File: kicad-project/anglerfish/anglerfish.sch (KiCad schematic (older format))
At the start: 3 parts

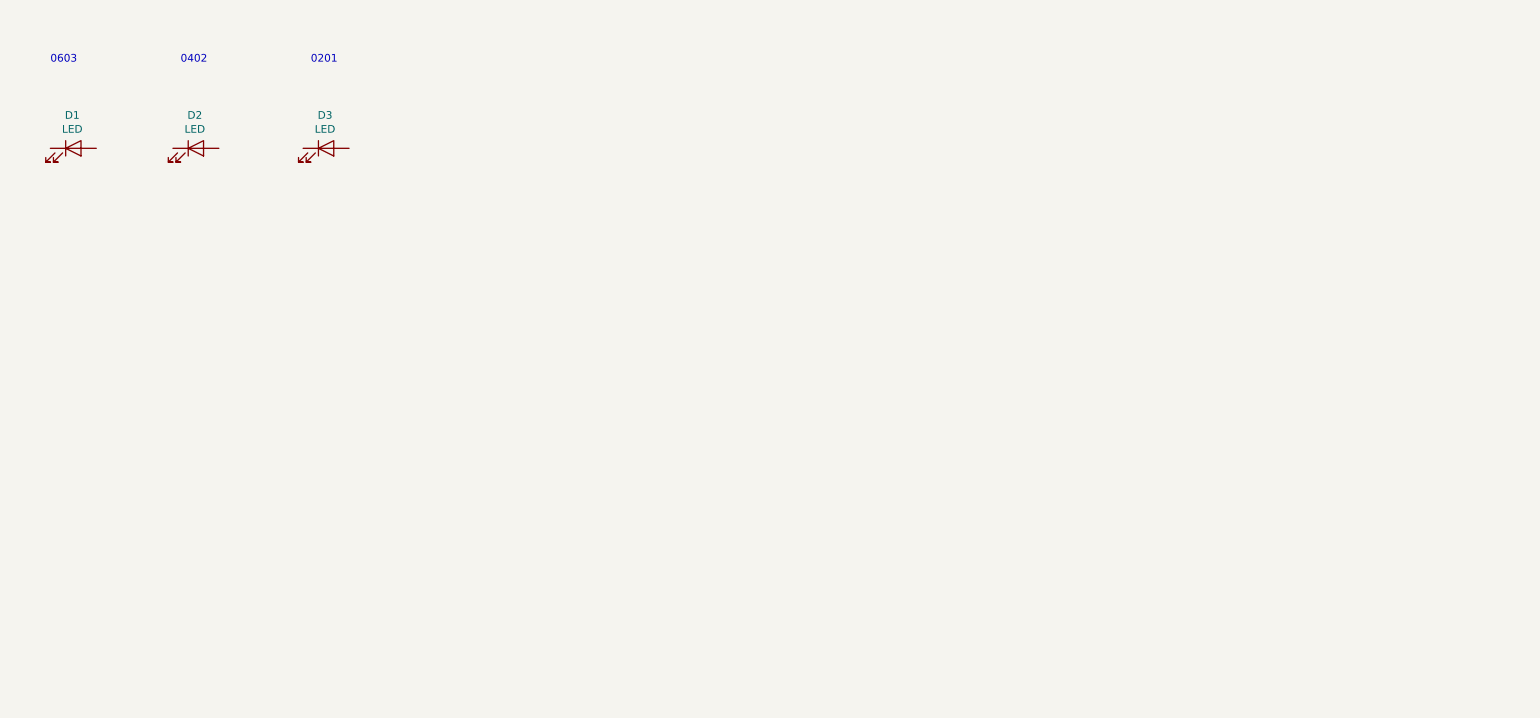
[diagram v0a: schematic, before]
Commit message: Added the 0402 whites. Also added the APA.
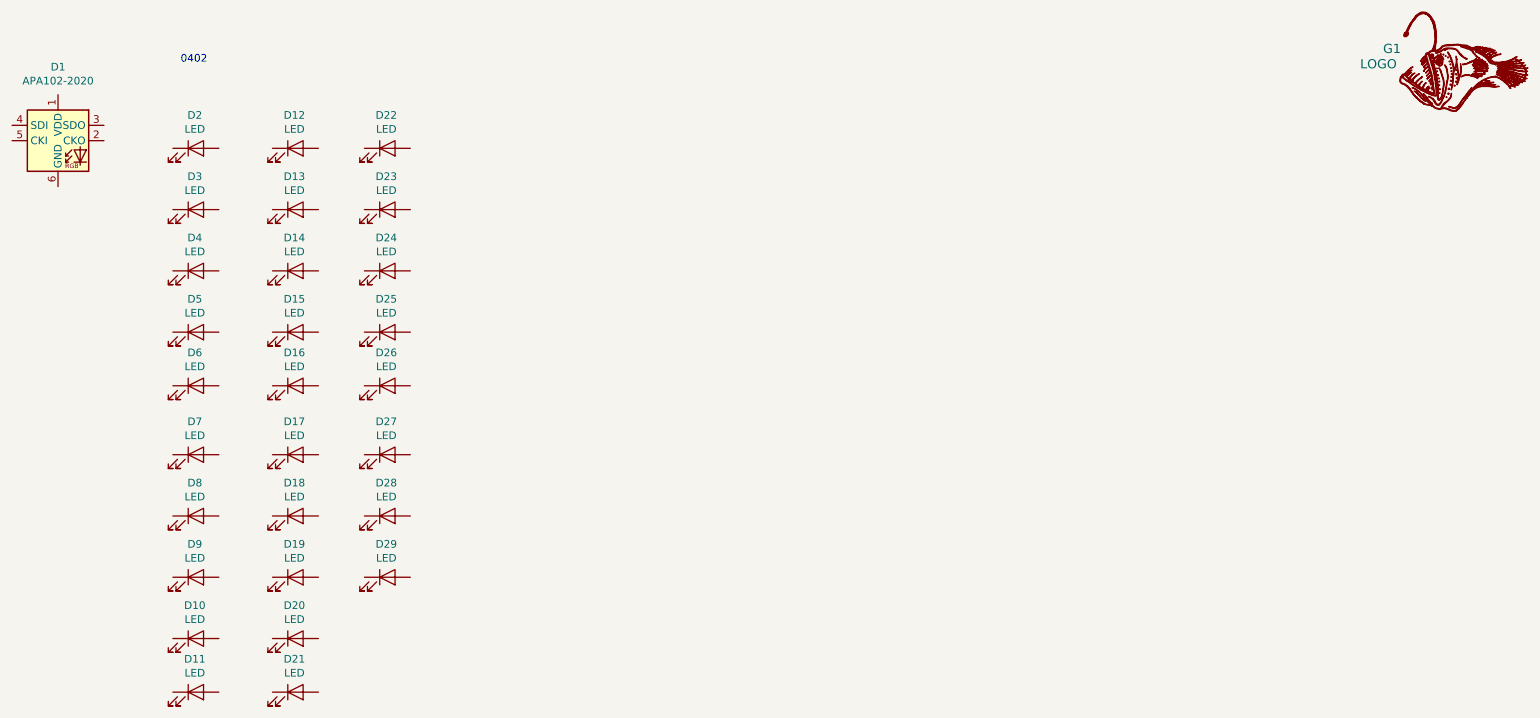
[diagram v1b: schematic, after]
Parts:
- removed D1: LED, LED_SMD:LED_0603_1608Metric, symbol Device:LED
- added D1: APA102-2020, LED_SMD:LED-APA102-2020, symbol LED:APA102-2020
- added D10, D11, D12, D13, D14, D15, D16, D17, D18, D19, D20, D21, D22, D23, D24, D25, D26, D27, D28, D29, D4, D5, D6, D7, D8, D9: LED, LED_SMD:LED_0402_1005Metric, symbol Device:LED
- added G1: LOGO, kicad-lib:anglerfish, symbol anglerfish:LOGO
- D3: footprint LED_SMD:LED_0201_0603Metric -> LED_SMD:LED_0402_1005Metric
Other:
- note removed: "0201"
- note removed: "0603"

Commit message: Added the photodiode.
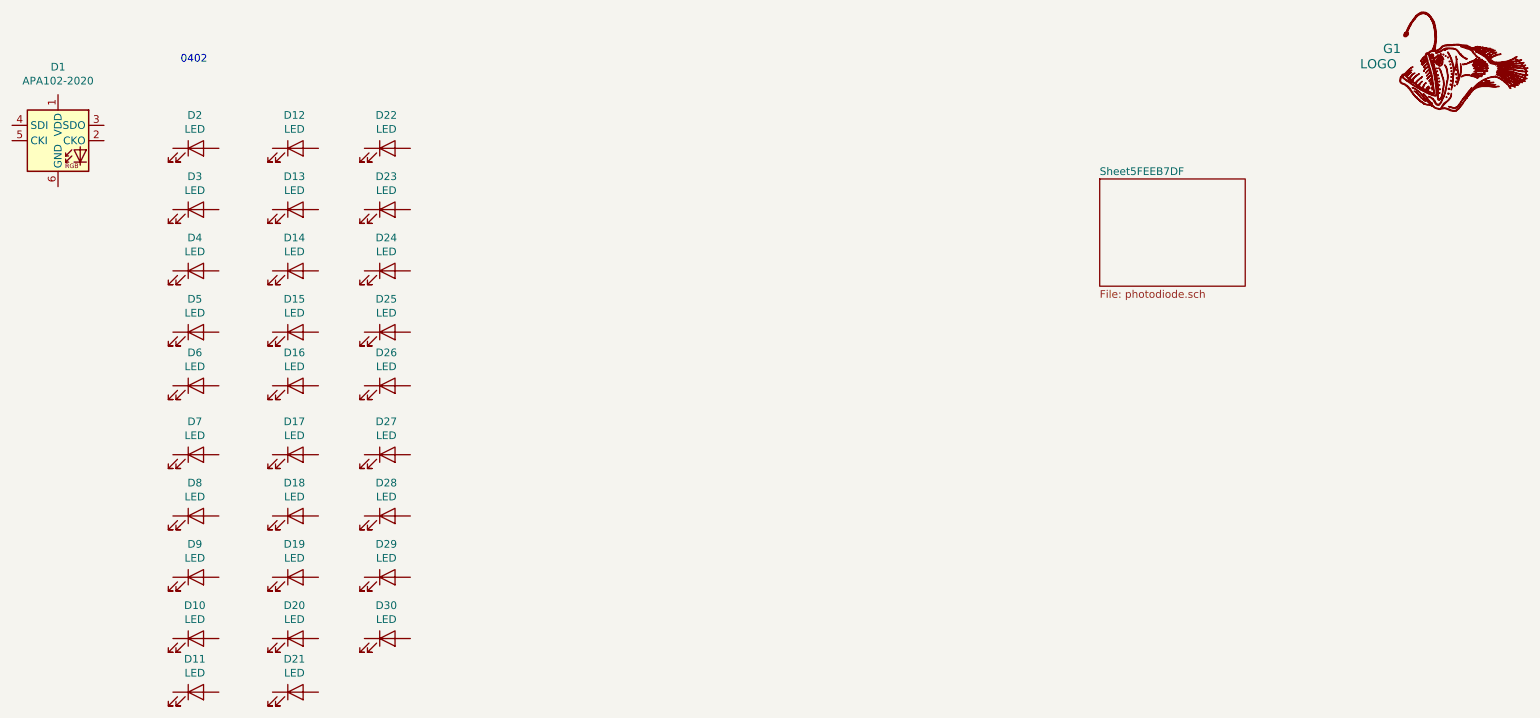
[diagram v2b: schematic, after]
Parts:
- added D30: LED, LED_SMD:LED_0402_1005Metric, symbol Device:LED
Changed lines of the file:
@@
 $Descr A4 11693 8268
 encoding utf-8
-Sheet 1 1
+Sheet 1 2
 Title ""
 Date ""
@@
 	1    0    0    -1
 $EndComp
+$Sheet
+S 8250 1700 950  700
+U 5FEEB7E0
+F0 "Sheet5FEEB7DF" 50
+F1 "photodiode.sch" 50
+$EndSheet
+$Comp
+L Device:LED D30
+U 1 1 5FEF7875
+P 3600 4700
+F 0 "D30" H 3593 4916 50  0000 C CNN
+F 1 "LED" H 3593 4825 50  0000 C CNN
+F 2 "LED_SMD:LED_0402_1005Metric" H 3600 4700 50  0001 C CNN
+F 3 "~" H 3600 4700 50  0001 C CNN
+	1    3600 4700
+	1    0    0    -1
+$EndComp
